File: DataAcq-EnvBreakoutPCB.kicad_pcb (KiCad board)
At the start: 2 copper layers, 19.4 x 27.2 mm, 22 parts, among them J4 Breakout Connector, U1 FS3000-1005, U2 LMT87DCK, U3 SHT45

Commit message: todos
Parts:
- removed C1, C2, C4, C5, C7: 0.1uF, Capacitor_SMD:C_0805_2012Metric
- removed C3, C6: 1uF, Capacitor_SMD:C_0805_2012Metric
- removed D1: VDDA, LED_SMD:LED_0805_2012Metric
- removed D2: 3.3V, LED_SMD:LED_0805_2012Metric
- removed G*** (x2): LOGO, LOGO
- removed H1, H2: M3, MountingHole:MountingHole_3mm
- removed J4: Breakout Connector, Connector_Molex:Molex_Nano-Fit_105310-xx10_2x05_P2.50mm_Vertical
- removed LOGO1: Arrow, images:arrow
- removed LOGO3: UTSVT Logo, images:utsvt_small
- removed R1: 1k, Resistor_SMD:R_0805_2012Metric
- removed R2, R3: 2.2k, Resistor_SMD:R_0805_2012Metric
- removed U1: FS3000-1005, SamacSys_Parts:FS30001005
- removed U2: LMT87DCK, Package_TO_SOT_SMD:SOT-353_SC-70-5
- removed U3: SHT45, Sensor_Humidity:Sensirion_DFN-4_1.5x1.5mm_P0.8mm_SHT4x_NoCentralPad
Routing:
- net /I2C1_SCL: track 17.2 -> 0.00 mm, vias 2 -> 0
- net VDDA: track 16.4 -> 0.00 mm, vias 2 -> 0
- net /I2C1_SDA: track 16.1 -> 0.00 mm, vias 2 -> 0
- net GNDA: track 14.8 -> 0.00 mm, vias 2 -> 0
- net /PA1(ADC): track 11.4 -> 0.00 mm, vias 2 -> 0
- net /I2C2_SCL: track 5.49 -> 0.00 mm, vias 1 -> 0
- net /I2C2_SDA: track 4.98 -> 0.00 mm
- net /AFLW_TP1: track 2.29 -> 0.00 mm, vias 1 -> 0
- net Net-(D2-A): track 2.27 -> 0.00 mm
- net Net-(D1-A): track 2.26 -> 0.00 mm
- net /AFLW_VCM: track 2.06 -> 0.00 mm, vias 1 -> 0
- net /AFLW_TP2: track 2.03 -> 0.00 mm, vias 1 -> 0
- net /AFLW_VREG: track 2.01 -> 0.00 mm, vias 1 -> 0
- net /TEMP_OUT: track 1.39 -> 0.00 mm, vias 1 -> 0
- net +3.3V: track 1.37 -> 0.00 mm, vias 2 -> 0
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- removed copper zone on B.Cu, net +3.3V
- removed copper zone on F.Cu, net GND
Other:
- board outline removed
- board text removed: "3.3V"
- board text removed: "Airflow"
- board text removed: "Env Sensor Breakout"
- board text removed: "Grid size is .25mm"
- board text removed: "Humidity"
- board text removed: "MainConn"
- board text removed: "Ravi Shah 2024"
- board text removed: "Temp"
- board text removed: "VDDA"

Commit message: footprints, component models, P/N
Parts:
- added C1: 0.1u, Capacitor_SMD:C_0603_1608Metric, F.Cu at (147.4, 88.8)
- added C2: 0.1u, Capacitor_SMD:C_0603_1608Metric, F.Cu at (147.4, 91.3)
- added C3: 0.1u, Capacitor_SMD:C_0603_1608Metric, F.Cu at (147.4, 93.8)
- added C4: 1u, Capacitor_SMD:C_0603_1608Metric, F.Cu at (147.4, 96.3)
- added C5: 0.1u, Capacitor_SMD:C_0603_1608Metric, F.Cu at (147.4, 98.8)
- added C6: 0.1u, Capacitor_SMD:C_0603_1608Metric, F.Cu at (147.4, 101.3)
- added C7: 0.1u, Capacitor_SMD:C_0603_1608Metric, F.Cu at (147.4, 103.8)
- added C8: 10u, Capacitor_SMD:C_0603_1608Metric, F.Cu at (147.4, 106.3)
- added D1: PWR, LED_SMD:LED_0805_2012Metric, F.Cu at (167.1, 113.0)
- added D2: PESD3V3L4BHCYL, PESD3V3L4BHCYL:SON45P80X130X43-6N, F.Cu at (155.1, 114.8)
- added H1: M3, MountingHole:MountingHole_3mm, F.Cu at (153.2, 91.3)
- added H2: M3, MountingHole:MountingHole_3mm, F.Cu at (153.2, 98.8)
- added J1: ENV, 1053091104`:MOLEX_1053091104, F.Cu at (160.5, 91.1)
- added LOGO1: Arrow, images:arrow, F.Cu at (159.4, 111.6)
- added LOGO3: UTSVT Logo, images:utsvt_small, F.Cu at (167.9, 110.1)
- added R1: 680, Capacitor_SMD:C_0603_1608Metric, F.Cu at (147.4, 108.9)
- added TP1: 3.3V, TestPoint:TestPoint_Pad_1.0x1.0mm, F.Cu at (172.5, 105.5)
- added TP2: GND, TestPoint:TestPoint_Pad_1.0x1.0mm, F.Cu at (177.2, 105.5)
- added U1: FS3000-1005, SamacSys_Parts:FS30001005, F.Cu at (163.0, 103.0)
- added U2: MPL3115A2ST1, Package_LGA:NXP_LGA-8_3x5mm_P1.25mm_H1.1mm, F.Cu at (152.3, 105.9)
- added U3: SHT45, Sensor_Humidity:Sensirion_DFN-4_1.5x1.5mm_P0.8mm_SHT4x_NoCentralPad, F.Cu at (151.4, 110.7)
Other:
- copper layers 2 -> 4

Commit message: layout kinda
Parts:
- C1, C3, C4, C5, C6, C7, C8: footprint Capacitor_SMD:C_0603_1608Metric -> Capacitor_SMD:C_0805_2012Metric; moved to B.Cu
- C2: footprint Capacitor_SMD:C_0603_1608Metric -> Capacitor_SMD:C_0805_2012Metric
- R1: footprint Capacitor_SMD:C_0603_1608Metric -> Resistor_SMD:R_0805_2012Metric
- moved U1 65.3 mm to (105.0, 73.0)
- moved D2 57.0 mm to (114.5, 74.8)
- moved U3 54.5 mm to (112.0, 73.2), turned to 180 degrees
- moved H1 54.1 mm to (100.0, 81.2)
- moved U2 52.9 mm to (106.0, 80.5), turned to -90 degrees
- moved C8 52.8 mm to (104.6, 75.3)
- moved C2 52.5 mm to (98.5, 72.3), turned to -90 degrees
- moved C4 50.3 mm to (103.2, 72.3), turned to -90 degrees
- moved C1 50.2 mm to (100.0, 72.3), turned to -90 degrees
- moved C7 50.2 mm to (104.6, 77.6)
- moved C6 47.3 mm to (104.6, 81.3), turned to 180 degrees
- moved C3 47.1 mm to (105.5, 72.3), turned to 90 degrees
- moved H2 44.6 mm to (112.2, 81.2)
- moved J1 43.5 mm to (118.8, 78.8), turned to 90 degrees
- moved C5 43.1 mm to (112.7, 73.2), turned to -90 degrees
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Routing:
- net /I2C1_SCL: track 0.00 -> 4.10 mm, vias 0 -> 1
- net GND: track 0.00 -> 3.15 mm
- net +3.3V: track 0.00 -> 1.36 mm, vias 0 -> 1
- added copper zone on B.Cu, net +3.3V
- added copper zone on In1.Cu, net +3.3V
- added copper zone on F.Cu, net GND
- added copper zone on In2.Cu, net GND
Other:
- board outline added: 25.2 x 17.5 mm
- board text added: "STITCHING VIASSSSSS"

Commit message: routing
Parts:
- R1, TP1: moved to B.Cu
- moved TP2 87.6 mm to (112.8, 69.8)
- moved TP1 73.4 mm to (117.5, 81.5), turned to 180 degrees
- moved D1 62.1 mm to (98.5, 76.2), turned to -90 degrees
- moved R1 58.8 mm to (98.5, 76.2), turned to -90 degrees
- moved C5 3.45 mm to (109.2, 73.2)
- moved H1 0.25 mm to (99.8, 81.2)
- moved U3 0.20 mm to (111.8, 73.2)
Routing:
- net /I2C1_SDA: track 0.00 -> 23.3 mm, vias 0 -> 4
- net /I2C1_SCL: track 4.10 -> 22.5 mm, vias 1 -> 4
- net GND: track 3.15 -> 17.7 mm, vias 0 -> 4
- net +3.3V: track 1.36 -> 11.9 mm, vias 1 -> 5
- net /VCM: track 0.00 -> 5.36 mm, vias 0 -> 1
- net /TP2: track 0.00 -> 2.93 mm, vias 0 -> 1
- net /TP1: track 0.00 -> 2.85 mm, vias 0 -> 1
- net /VREG: track 0.00 -> 2.53 mm, vias 0 -> 1
- net /CAP: track 0.00 -> 2.53 mm, vias 0 -> 1
- net Net-(D1-A): vias 0 -> 1
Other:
- board size 25.2 x 17.5 mm -> 25.2 x 16.8 mm

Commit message: stitching/fixes
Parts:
- added G***: LOGO, LOGO, F.Cu at (118.2, 82.8)
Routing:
- net GND: track 17.7 -> 17.8 mm, vias 4 -> 12
- net +3.3V: vias 5 -> 15
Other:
- board text added: "Ravi Shah 2025"
- board text removed: "STITCHING VIASSSSSS"

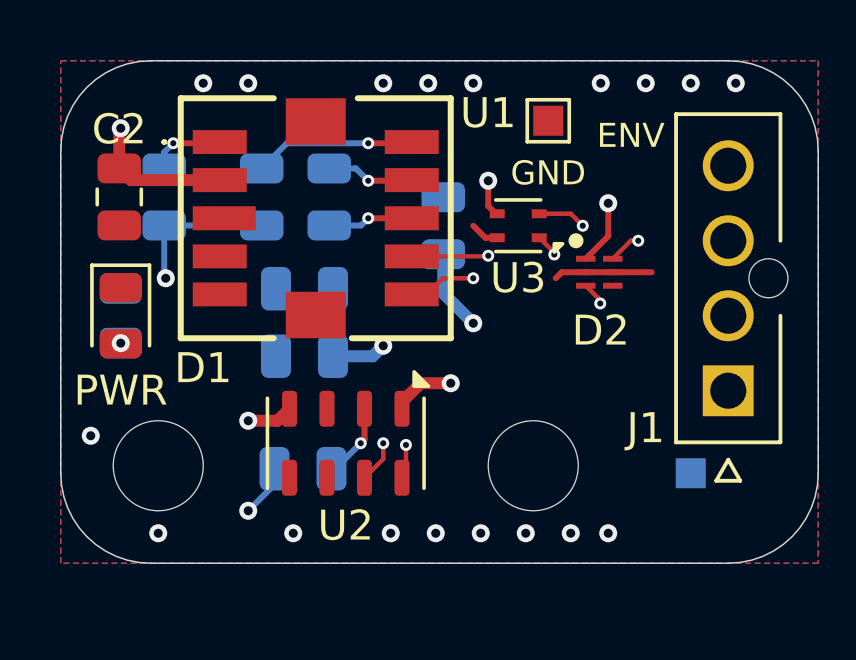
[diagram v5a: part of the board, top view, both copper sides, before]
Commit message: fix via sizes for jlc bs
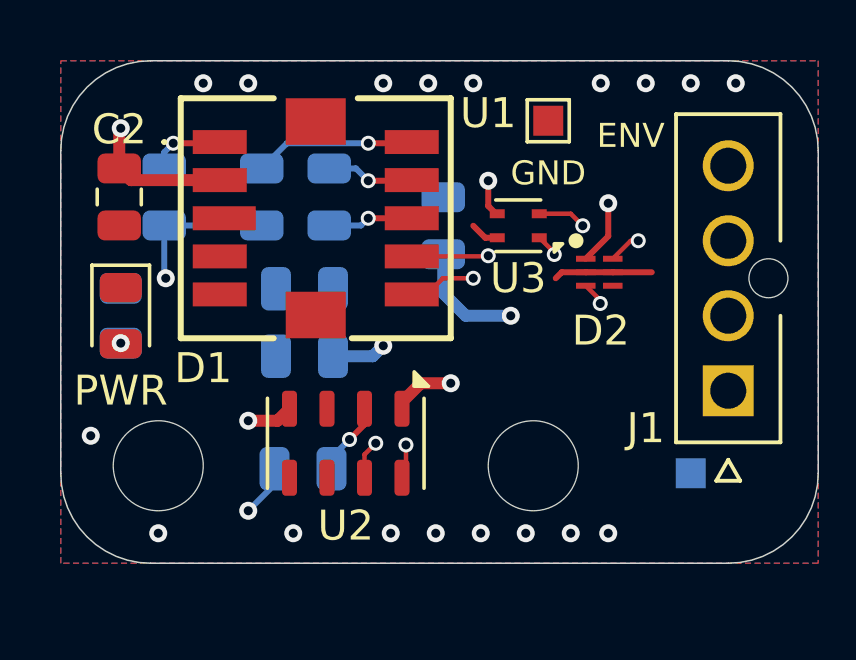
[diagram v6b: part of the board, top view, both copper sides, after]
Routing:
- net GND: track 17.8 -> 19.0 mm
